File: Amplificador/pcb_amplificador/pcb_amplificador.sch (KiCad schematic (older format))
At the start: 123 parts, among them CON1 SJ-3523-SMT-TR, J1 Screw_Terminal_01x02, J2 Conn_01x03_Male, J3 Screw_Terminal_01x06, K1 SANYOU_SRD_Form_B, M1 FDS9934C, M2 FDS9934C, M3 FDS9934C, Q1 BC860, Q10 BD139, Q11 BD140, Q12 BD139, Q13 2SA1943-O_Q_, Q14 2SC5200-O_Q, Q15 2SA1943-O_Q_, Q16 2SC5200-O_Q, Q17 2SAR514P5, Q18 BC860, Q19 BC860, Q2 BC860, Q20 2SAR514P5, Q21 2SCR514P5, Q22 2SCR514P5, Q23 2SCR514P5, Q24 2SAR514P5, Q25 2SCR514P5, Q26 BC817, Q27 BC817, Q28 BC807, Q3 BC850, Q4 BC850, Q5 BC860, Q6 BC860, Q7 BC850, Q8 2SCR514P5, Q9 2SCR514P5

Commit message: Cambios en el esquematico del PCB
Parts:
- removed J3: Screw_Terminal_01x06, Connector_Phoenix_MC:PhoenixContact_MCV_1,5_6-G-3.5_1x06_P3.50mm_Vertical, symbol Connector:Screw_Terminal_01x06
- removed R100: 680, Resistor_SMD:R_0805_2012Metric_Pad1.15x1.40mm_HandSolder, symbol Device:R
- added C15: 10u, Capacitor_SMD:C_0805_2012Metric_Pad1.15x1.40mm_HandSolder, symbol Device:C
- added J1, J2, J3: Screw_Terminal_01x02, Connector_Phoenix_MC:PhoenixContact_MCV_1,5_2-G-3.5_1x02_P3.50mm_Vertical, symbol Connector:Screw_Terminal_01x02
- C5, C9: value 10u -> 100u
- R29, R33: value 1k -> 5k
- renumbered J1 to J4, J2 to J5
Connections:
- net -Vmax: now also J2.2 (Pin_2)
- net -Vmin: now also J1.2 (Pin_2)
- net Earth: now also CON1.3 (R), J3.1 (Pin_1), J3.2 (Pin_2); no longer CON1.1 (S), J4.2 (Pin_2)
- net Vmax: now also J2.1 (Pin_1)
- net Vmin: now also J1.1 (Pin_1)
- net at C2.2, R25.1, R26.2: now also C15.2
- net at C2.1, R24.2: now also C15.1
- no-connect marks 1 -> 3
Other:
- moved on the sheet: Q23, Q24, R25, R42

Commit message: Primer diseño completo de todo el PCB del amplificador
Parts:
- removed C5, C9: 100u, Capacitor_SMD:C_1206_3216Metric_Pad1.42x1.75mm_HandSolder, symbol Device:C
- removed M3: FDS9934C, Package_SO:SOIC-8_3.9x4.9mm_P1.27mm, symbol Transistor_FET:FDS9934C
- added C5, C9: 100u, Capacitor_SMD:CP_Elec_8x10.5, symbol Device:CP
- added HS1: Heatsink, disipadores:disipador_1.8C, symbol Mechanical:Heatsink
- added HS2: Heatsink, disipadores:disipador_5.1C, symbol Mechanical:Heatsink
- added J6, J7: Screw_Terminal_01x02, Connector_Phoenix_MC:PhoenixContact_MCV_1,5_2-G-3.5_1x02_P3.50mm_Vertical, symbol Connector:Screw_Terminal_01x02
- added Q29: BS170, Package_TO_SOT_THT:TO-92_Inline, symbol Transistor_FET:BS170
- added R33, R48: 10k, Resistor_SMD:R_0805_2012Metric_Pad1.15x1.40mm_HandSolder, symbol Device:R
- added R52, R53, R54, R55, R56, R57, R59, R60, R61, R62, R63, R64: 0, Resistor_SMD:R_1206_3216Metric_Pad1.42x1.75mm_HandSolder, symbol Device:R
- C2: footprint Capacitor_SMD:CP_Elec_10x10.5 -> Capacitor_SMD:CP_Elec_8x10.5
- R29: value 5k -> 10k
- R49: renamed from R33; value 5k -> 10k
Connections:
- net -Vmax: now also C8.2, J2.1 (Pin_1), J6.1 (Pin_1), R48.1; no longer C8.1, J2.2 (Pin_2)
- net -Vmin: now also J2.2 (Pin_2), R5.2, R53.2; no longer J1.2 (Pin_2), R35.2
- net Earth: now also C10.2, C8.1, C5.1, C9.2, Q29.3 (S); no longer C10.1, C8.2
- net Vmax: now also C10.1, J1.2 (Pin_2), J7.2 (Pin_2), R33.1, R64.2; no longer C10.2, J2.1 (Pin_1), R37.2
- net Vmin: now also R54.2; no longer K1.5, R5.2, R50.2
- net at Q25.3 (E), R3.2, R4.2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: now also C5.2
- net at C7.2, Q18.2 (E), R17.2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: now also C9.1
- net at C13.1, Q26.3 (C), Q28.2 (E)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: now also Q29.2 (G)
- net at R10.1, R13.1: now also R52.2; no longer Q17.2 (C)
- net at M2.1 (S), Q11.1 (E), R14.1: now also R57.2; no longer M1.1 (S), R34.1
- net at M1.3 (1), Q12.1 (E), R14.2: now also R56.2; no longer M2.3 (1), R30.1
- net at K1.2: now also Q29.1 (D)
- net at D9.2 (A), Q15.1 (B), Q23.2 (C)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: now also R33.2, R61.2; no longer M1.7 (D), M1.8 (D), M2.2 (G)
- net at D3.1 (K), M2.5 (D), M2.6 (D)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: now also R48.2, R59.2, R63.1; no longer M1.4 (G), Q24.2 (C)
- net at M1.2 (G), R34.2: now also R55.1; no longer D13.1 (K), Q21.2 (C)
- new net: K1.5, R50.2, R54.1
- new net: M2.3 (1), R30.1, R56.1
- new net: D13.1 (K), Q21.2 (C), R55.2
- new net: M1.1 (S), R34.1, R57.1
- new net: R35.2, R53.1
- new net: Q17.2 (C), R52.1
- new net: Q24.2 (C), R63.2
- new net: M1.4 (G), R60.1
- new net: R59.1, R60.2
- new net: M1.7 (D), M1.8 (D), M2.2 (G), R62.1
- new net: R61.1, R62.2
- new net: R37.2, R64.1
- no-connect marks 3 -> 5
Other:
- moved on the sheet: D13, R10, R12, R13, R29, R37, R49

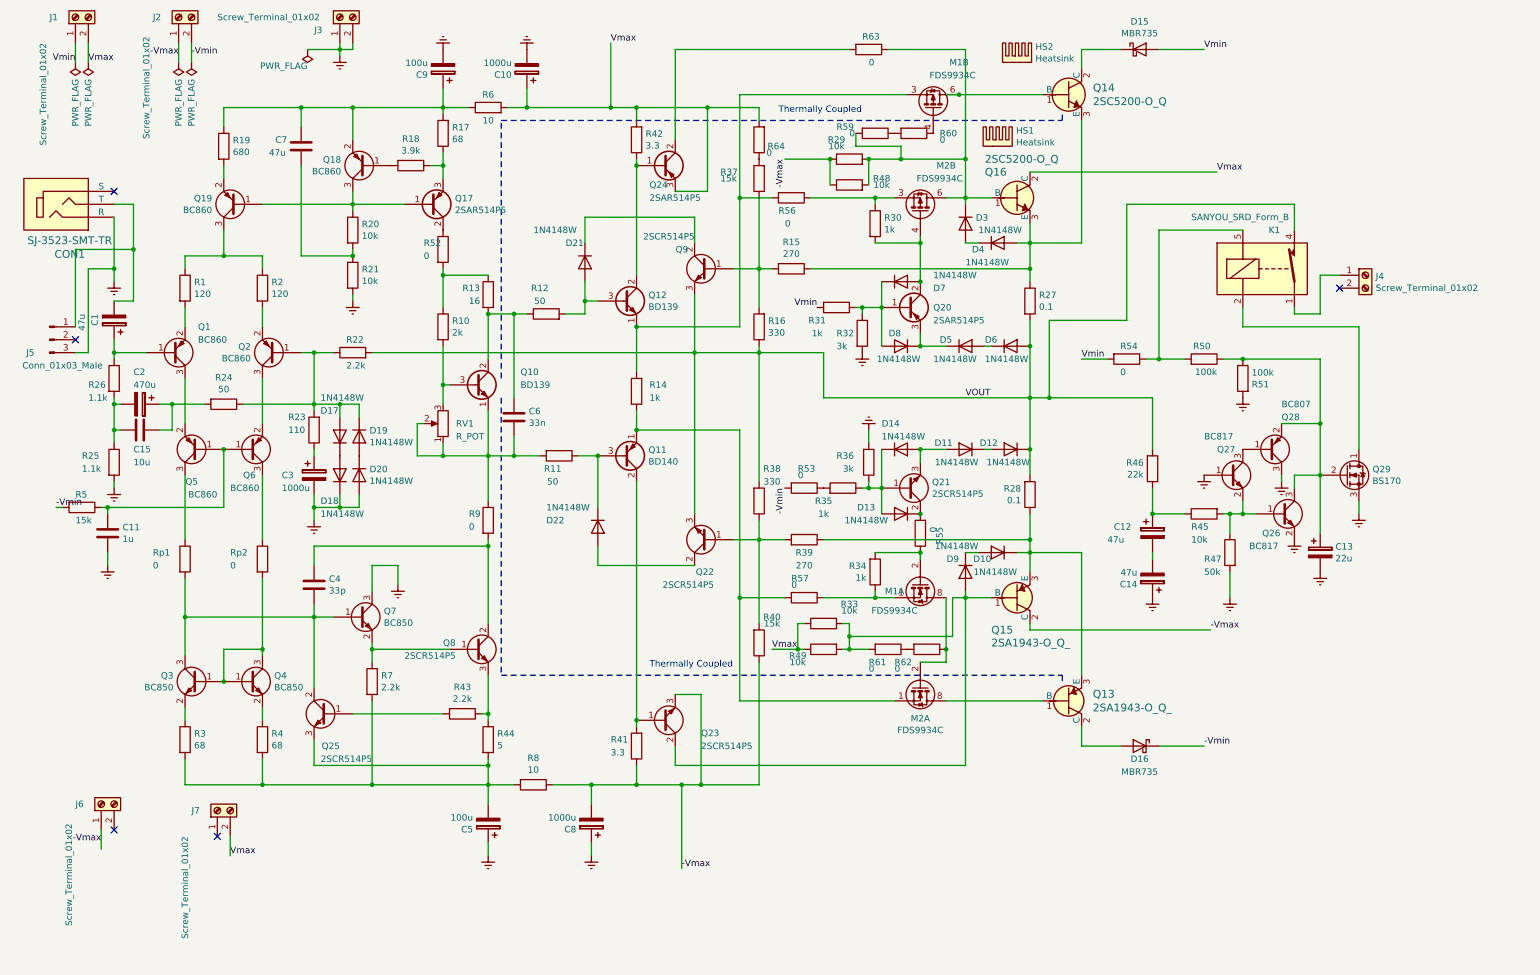
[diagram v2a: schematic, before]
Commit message: Se mueve el contenido sobre PCB de la rama PCB_review a develop
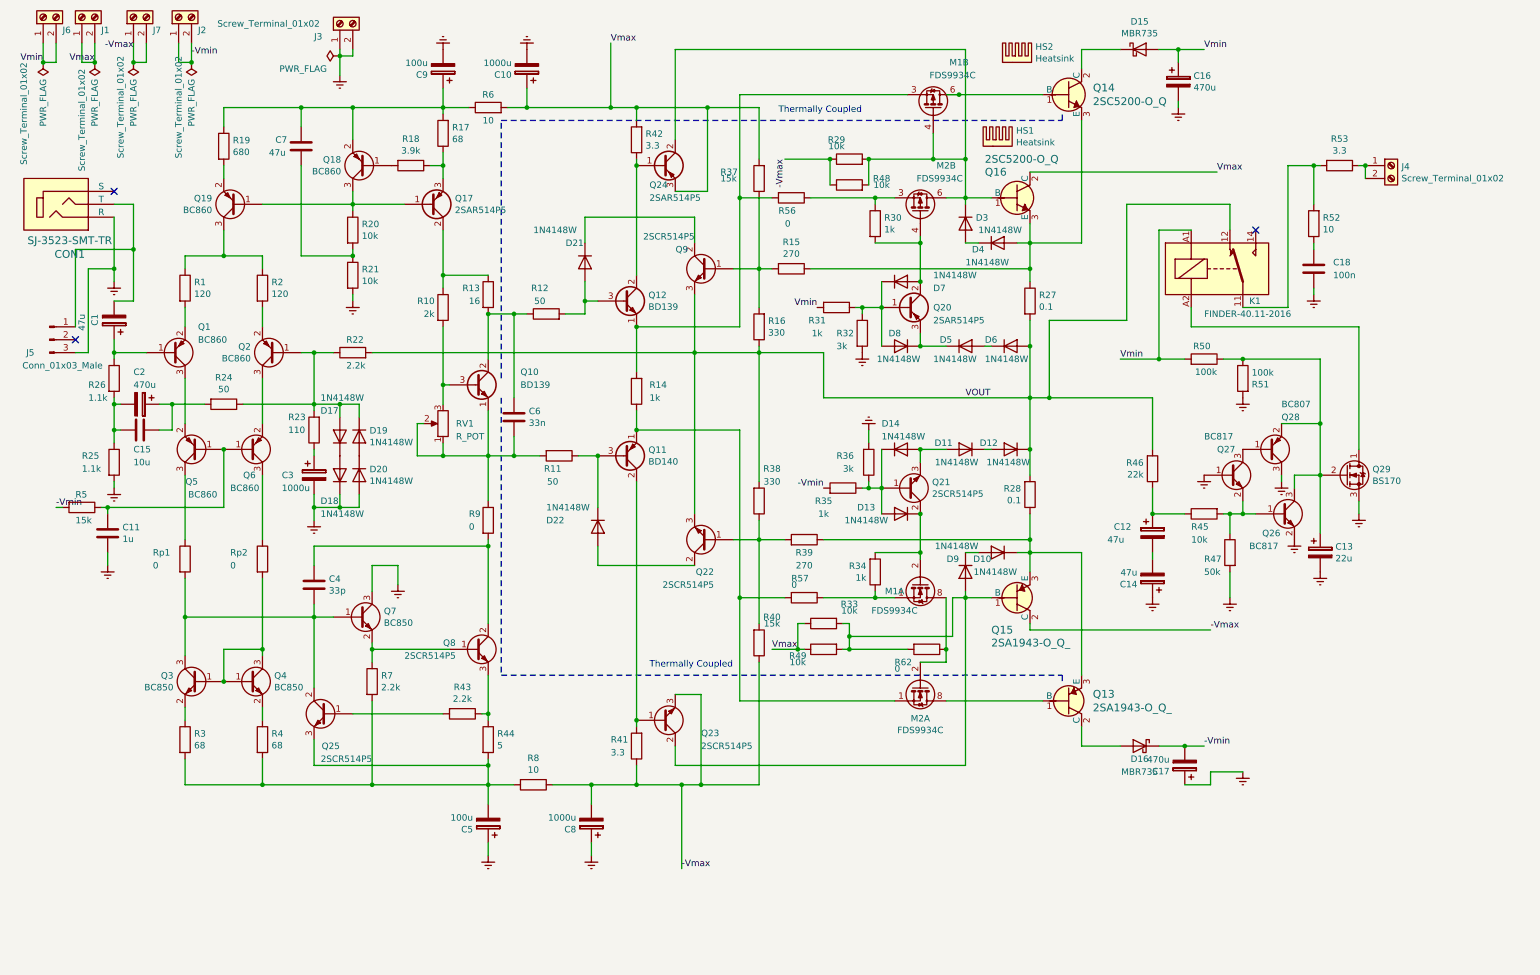
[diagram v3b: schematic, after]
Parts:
- removed K1: SANYOU_SRD_Form_B, Relay_THT:Relay_SPST_SANYOU_SRD_Series_Form_B, symbol pcb_amplificador-rescue:SANYOU_SRD_Form_B-Relay
- removed R54, R55, R59, R60, R61, R63, R64: 0, Resistor_SMD:R_1206_3216Metric_Pad1.42x1.75mm_HandSolder, symbol Device:R
- added C16, C17: 470u, Capacitor_THT:CP_Radial_D12.5mm_P5.00mm, symbol Device:CP
- added C18: 100n, Capacitor_THT:C_Disc_D7.5mm_W5.0mm_P7.50mm, symbol Device:C
- added K1: FINDER-40.11-2016, Relay_THT:Relay_SPDT_Schrack-RP-II-1-16A-FormC_RM5mm, symbol Relay:FINDER-40.11-2016
- Q1, Q18, Q19, Q2, Q26, Q27, Q28, Q3, Q4, Q5, Q6, Q7: footprint Package_TO_SOT_SMD:SOT-23 -> Package_TO_SOT_SMD:SOT-23_Handsoldering
- Q17, Q20, Q21, Q22, Q23, Q24, Q25, Q8, Q9: footprint Package_TO_SOT_SMD:SOT-89-3 -> Package_TO_SOT_SMD:SOT-89-3_Handsoldering
- R27, R28: footprint Resistor_SMD:R_2512_6332Metric_Pad1.52x3.35mm_HandSolder -> Resistor_THT:R_Axial_DIN0411_L9.9mm_D3.6mm_P12.70mm_Horizontal
- R52: value 0 -> 10; footprint Resistor_SMD:R_1206_3216Metric_Pad1.42x1.75mm_HandSolder -> Resistor_THT:R_Axial_DIN0614_L14.3mm_D5.7mm_P15.24mm_Horizontal
- R53: value 0 -> 3.3; footprint Resistor_SMD:R_1206_3216Metric_Pad1.42x1.75mm_HandSolder -> Resistor_THT:R_Axial_DIN0207_L6.3mm_D2.5mm_P7.62mm_Horizontal
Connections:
- net -Vmax: now also J7.1 (Pin_1), J7.2 (Pin_2); no longer J2.1 (Pin_1), J6.1 (Pin_1)
- net -Vmin: now also J2.1 (Pin_1), R35.2, C17.2; no longer R53.2
- net Earth: now also C16.2, C17.1, C18.1
- net VOUT: now also K1.12
- net Vmax: now also J1.1 (Pin_1), R37.2; no longer J7.2 (Pin_2)
- net Vmin: now also J6.1 (Pin_1), J6.2 (Pin_2), R50.2, C16.1, K1.A1; no longer J1.1 (Pin_1)
- net at R10.1, R13.1: now also Q17.2 (C); no longer R52.2
- net at J4.1 (Pin_1): now also J4.2 (Pin_2), R53.1
- net at Q29.1 (D): now also K1.A2
- net at D9.2 (A), Q15.1 (B), Q23.2 (C)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: now also R62.2
- net at D3.1 (K), M2.5 (D), M2.6 (D)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: now also M1.4 (G), Q24.2 (C)
- net at M1.2 (G), R34.2: now also D13.1 (K), Q21.2 (C)
- net at R52.1: now also C18.2; no longer Q17.2 (C)
- new net: K1.11, R52.2, R53.2
- no-connect marks 5 -> 3
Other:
- moved on the sheet: J1, J3, J4, R10

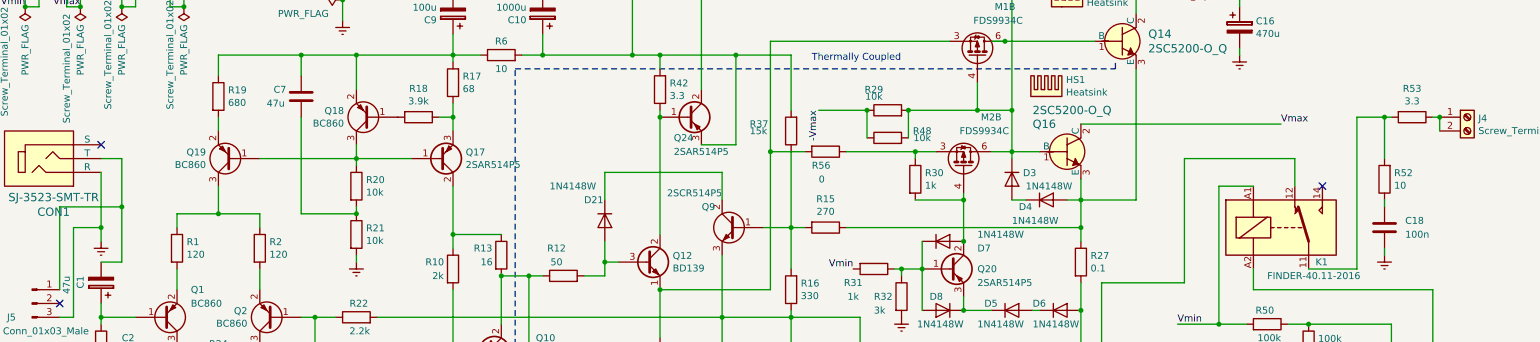
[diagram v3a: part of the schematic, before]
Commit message: Actualización de las especificaciones del amplificador
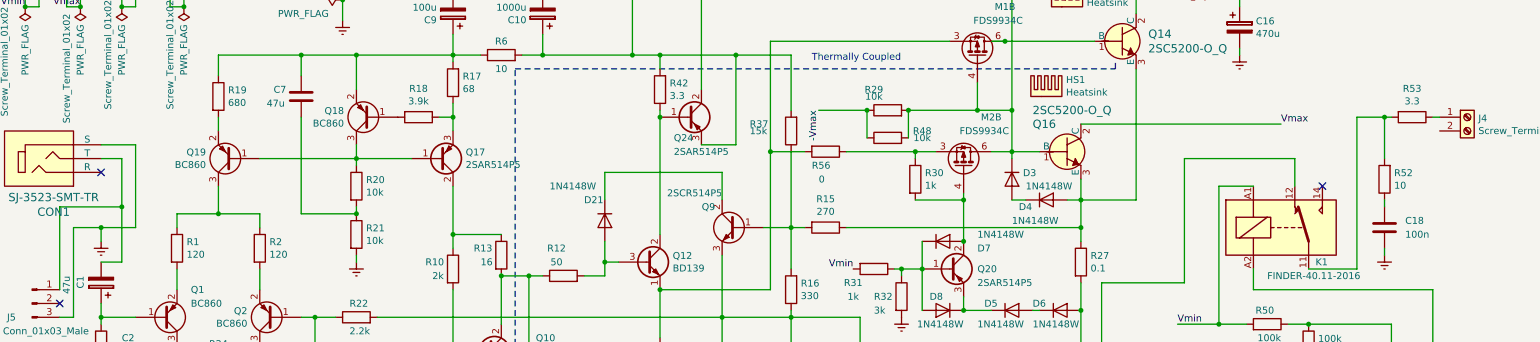
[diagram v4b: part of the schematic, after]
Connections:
- net Earth: now also CON1.1 (S); no longer CON1.3 (R)
- net at J4.1 (Pin_1), R53.1: no longer J4.2 (Pin_2)
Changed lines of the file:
@@
 	1400 2000 1400 2350
-Wire Wire Line
-	1250 2100 1250 2500
 Wire Wire Line
 	950  2950 950  2350
@@
 Wire Wire Line
 	1050 2500 1250 2500
-Connection ~ 1250 2500
 Wire Wire Line
 	1250 2500 1250 2600
@@
 	0    -1   1    0
 $EndComp
-NoConn ~ 1250 1900
 Wire Wire Line
 	1100 750  1100 900
@@
 Wire Wire Line
 	10550 1700 10350 1700
-Connection ~ 10950 1700
-Wire Wire Line
-	10950 1800 10950 1700
 Wire Wire Line
 	6950 5450 7400 5450
@@
 	0    1    1    0
 $EndComp
+Wire Wire Line
+	1250 1900 1500 1900
+Wire Wire Line
+	1500 1900 1500 2500
+Wire Wire Line
+	1500 2500 1250 2500
+Connection ~ 1250 2500
+NoConn ~ 1250 2100
 $EndSCHEMATC
